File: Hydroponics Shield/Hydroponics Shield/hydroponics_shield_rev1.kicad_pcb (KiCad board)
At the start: 2 copper layers, 125 x 64.5 mm, 50 parts, among them CON1 BARREL_JACK, J1 282836-6, J2 282836-6, P1 CONN_01X02, P2 CONN_01X03, P3 CONN_01X04, P4 CONN_01X02, P5 CONN_01X02, P9 0731000105, Q1 2N7000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

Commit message: desktop night changes
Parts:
- moved C2 133.6 mm to (137.7, 82.5), turned to 270 degrees
- moved R17 132.9 mm to (134.4, 95.0)
- moved R18 129.8 mm to (144.5, 91.7), turned to 180 degrees
- moved C1 125.0 mm to (147.6, 92.7)
- moved U1 118.8 mm to (142.7, 88.9), turned to 90 degrees
- moved R13 108.2 mm to (134.4, 78.5)
- moved REF1 107.1 mm to (147.3, 98.3), turned to 0 degrees
- moved R12 98.3 mm to (144.5, 75.2), turned to 180 degrees
- moved R10 35.0 mm to (100.8, 115.1), turned to 0 degrees
- moved Q6 25.4 mm to (66.5, 97.5), turned to 180 degrees
- moved D3 25.2 mm to (31.0, 93.5), turned to 0 degrees
- moved Q5 24.2 mm to (81.8, 97.5), turned to 180 degrees
- moved Q8 23.6 mm to (36.1, 97.5), turned to 180 degrees
- moved Q7 23.0 mm to (51.3, 97.5), turned to 180 degrees
- moved R6 22.3 mm to (106.2, 88.6), turned to 90 degrees
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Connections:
- net Net-(P9-Pad2) renamed Vguard
- Q4 pad 1: Net-(PCB1-Pad3) -> Net-(PCB1-Pad2)
- R10 pad 2: Net-(PCB1-Pad2) -> Net-(PCB1-Pad3)
- R7 pad 1: Net-(PCB1-Pad3) -> Net-(PCB1-Pad2)
- R9 pad 1: Net-(PCB1-Pad2) -> Net-(PCB1-Pad3)
- SHIELD1 pad 10: DOSING_PUMP_2 -> DOSING_PUMP_1
- SHIELD1 pad 11: DOSING_PUMP_1 -> LED_STRIP_OUT
- SHIELD1 pad 6: LED_STRIP_OUT -> MAIN_PUMP
- SHIELD1 pad 9: MAIN_PUMP -> DOSING_PUMP_2
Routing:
- net MAIN_PUMP: track 0.00 -> 79.0 mm
- net DOSING_PUMP_2: track 0.00 -> 65.2 mm
- net BLE_DATA_TRANSMIT: track 0.00 -> 62.6 mm
- net Vguard: track 0.00 -> 61.3 mm
- net BLE_DATA_RECEIVE: track 0.00 -> 59.2 mm, vias 0 -> 1
- net DOSING_PUMP_1: track 0.00 -> 48.8 mm
- net LED_B: track 0.00 -> 30.5 mm, vias 0 -> 1
- net LED_STRIP_OUT: track 0.00 -> 29.7 mm
- net +5V: track 0.00 -> 25.3 mm
- net LED_R: track 0.00 -> 25.2 mm
- net LED_G: track 0.00 -> 20.2 mm, vias 0 -> 1
- net Net-(C1-Pad1): track 0.00 -> 17.9 mm
- net Net-(Q1-Pad3): track 0.00 -> 15.4 mm
- net PH_VOUT: track 0.00 -> 13.4 mm
- net Net-(Q2-Pad3): track 0.00 -> 10.8 mm
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- added copper zone on B.Cu, net GND
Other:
- board size 125 x 64.5 mm -> 125 x 62.2 mm

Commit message: workday additions
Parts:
- CON1: value BARREL_JACK -> PJ-202A
- P1, P4, P5: value CONN_01X02 -> 22-05-3021
- P2: value CONN_01X03 -> 0022053031
- P3: value CONN_01X04 -> 0022053041
- moved P5 53.2 mm to (148.3, 102.4), turned to 0 degrees
- moved J2 4.17 mm to (67.3, 64.3)
- moved J1 3.84 mm to (99.0, 64.3)
- moved CON1 3.49 mm to (36.3, 62.9)
- moved P9 3.05 mm to (149.1, 64.0)
- moved P4 2.34 mm to (108.2, 68.6)
- moved P2 2.34 mm to (122.4, 68.6)
- moved P3 2.30 mm to (132.3, 68.6)
- moved P1 2.29 mm to (115.3, 68.6)
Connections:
- J1 pad 1: GND -> +12V
- J1 pad 2: GND -> +12V
- J1 pad 3: GND -> +12V
- SHIELD1 pad AD0: PH_VOUT -> TEMP_SENSE_IN
- SHIELD1 pad AD1: PH_VREF -> PH_VOUT
- SHIELD1 pad AD2: TEMP_SENSE_IN -> Vguard
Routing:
- net +12V: track 0.00 -> 205.4 mm
- net +5V: track 25.3 -> 167.3 mm, vias 0 -> 3
- net AUX_BTTN1_IN: track 4.87 -> 105.2 mm, vias 0 -> 3
- net TEMP_SENSE_IN: track 0.00 -> 86.4 mm, vias 0 -> 4
- net PH_VOUT: track 13.4 -> 81.5 mm, vias 0 -> 1
- net Vguard: track 61.3 -> 120.3 mm, vias 0 -> 1
- net +3V3: track 0.00 -> 54.5 mm, vias 0 -> 2
- net Net-(J1-Pad4): track 0.00 -> 45.3 mm
- net Net-(C5-Pad2): track 0.00 -> 42.1 mm
- net Net-(C3-Pad2): track 0.90 -> 41.3 mm
- net Net-(C4-Pad2): track 0.00 -> 39.9 mm
- net Net-(PCB1-Pad2): track 5.75 -> 41.4 mm, vias 0 -> 2
- net GND: track 0.00 -> 24.7 mm, vias 0 -> 1
- net Net-(P3-Pad1): track 5.03 -> 21.2 mm, vias 1 -> 0
- net Net-(P3-Pad2): track 3.47 -> 19.7 mm
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- added copper zone on F.Cu, net GND
- added copper zone on B.Cu, net Vguard
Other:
- board size 125 x 62.2 mm -> 125 x 65.5 mm
- board text added: "+"
- board text added: "+12V IN"
- board text added: "-"
- board text added: "- OUT +"
- board text added: "AUX BTTN"
- board text added: "B G R A"
- board text added: "BTTN"
- board text added: "DOSING PUMP 1"
- board text added: "DOSING PUMP 2"
- board text added: "FLOAT SWITCH"
- board text added: "GROW LIGHTS"
- board text added: "HC05 Bluetooth Module"
- board text added: "HYDROPONICS SHIELD V0.1"
- board text added: "MAIN PUMP"
- board text added: "PH PROBE"
- board text added: "RGB LED"
- board text added: "TEMP SENSE"

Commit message: changes made extra pump wifi
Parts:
- added C6: 5ZLH100MEFC6.3X11, Capacitors_ThroughHole:C_Radial_D6.3_L11.2_P2.5, F.Cu at (65.0, 87.9)
- added D4: 1N4148, Diodes_ThroughHole:Diode_DO-35_SOD27_Horizontal_RM10, F.Cu at (61.0, 93.5)
- added Q9: PSMN022-30PL,127, TO_SOT_Packages_THT:TO-220_Neutral123_Horizontal_LargePads, F.Cu at (66.5, 97.5)
- added R22: 10.0k, Resistors_ThroughHole:Resistor_Horizontal_RM10mm, F.Cu at (102.9, 88.6)
- PCB1: value HC05_BLUETOOTH -> ESP8266; footprint USER_MODULES:HC05_BLUETOOTH_SMD -> USER_MODULES:ESP8266
- moved R16 19.8 mm to (83.1, 88.6)
- moved R9 17.0 mm to (126.2, 119.4)
- moved R7 16.2 mm to (126.2, 112.8)
- moved PCB1 15.9 mm to (131.8, 117.1), turned to 0 degrees
- moved R10 15.3 mm to (116.1, 116.1)
- moved C4 15.2 mm to (35.1, 87.9)
- moved C5 15.2 mm to (19.3, 87.9)
- moved D1 15.2 mm to (46.2, 93.5)
- moved D3 15.2 mm to (15.7, 93.5)
- moved Q6 15.2 mm to (51.3, 97.5)
- moved Q7 15.2 mm to (36.1, 97.5)
- moved D2 15.2 mm to (31.0, 93.5)
- moved Q8 15.2 mm to (20.8, 97.5)
- moved C3 15.2 mm to (50.3, 87.9)
- moved Q4 13.7 mm to (118.6, 105.7)
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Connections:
- net BLE_DATA_RECEIVE renamed WIFI_DATA_RECEIVE
- net BLE_DATA_TRANSMIT renamed WIFI_DATA_TRANSMIT
- J1 pad 3: +12V -> Net-(J1-Pad3)
- J1 pad 4: Net-(J1-Pad4) -> Net-(J1-Pad3)
- J1 pad 5: Net-(J1-Pad4) -> Net-(C6-Pad2)
- J1 pad 6: Net-(J1-Pad4) -> +12V
- PCB1 pad 1: Net-(PCB1-Pad1) -> GND
- PCB1 pad 4: GND -> +3V3
- PCB1 pad 5: +5V -> Net-(PCB1-Pad5)
- Q5 pad 2: Net-(J1-Pad4) -> Net-(J1-Pad3)
- R10 pad 2: Net-(PCB1-Pad3) -> Net-(PCB1-Pad7)
- R9 pad 1: Net-(PCB1-Pad3) -> Net-(PCB1-Pad7)
- SHIELD1 pad 12: Net-(SHIELD1-Pad12) -> MAIN_PUMP
- SHIELD1 pad 6: MAIN_PUMP -> TOPUP_PUMP
- SHIELD1 pad GND3: Net-(SHIELD1-PadGND3) -> GND
- SHIELD1 pad V_IN: Net-(SHIELD1-PadV_IN) -> +12V
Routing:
- net AUX_BTTN1_IN: track 105.2 -> 4.87 mm, vias 3 -> 0
- net +12V: track 205.4 -> 132.0 mm
- net TOPUP_PUMP: track 0.00 -> 48.4 mm
- net Net-(J1-Pad3): track 0.00 -> 47.8 mm
- net Net-(J1-Pad4): track 45.3 -> 0.00 mm
- net Net-(C6-Pad2): track 0.00 -> 44.2 mm
- net WIFI_DATA_RECEIVE: track 59.7 -> 34.1 mm, vias 1 -> 0
- net Net-(PCB1-Pad2): track 41.4 -> 19.1 mm, vias 2 -> 0
- net +5V: track 167.3 -> 149.2 mm, vias 3 -> 0
- net +3V3: track 54.5 -> 71.0 mm, vias 2 -> 0
- net DOSING_PUMP_1: track 48.8 -> 62.8 mm
- net DOSING_PUMP_2: track 65.2 -> 77.1 mm
- net WIFI_DATA_TRANSMIT: track 63.7 -> 52.6 mm
- net Net-(PCB1-Pad7): track 0.00 -> 10.8 mm
- net Net-(C5-Pad2): track 42.1 -> 52.6 mm
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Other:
- board size 125 x 65.5 mm -> 140.5 x 67.1 mm
- board text added: "TOP-UP PUMP"
- board text removed: "HC05 Bluetooth Module"

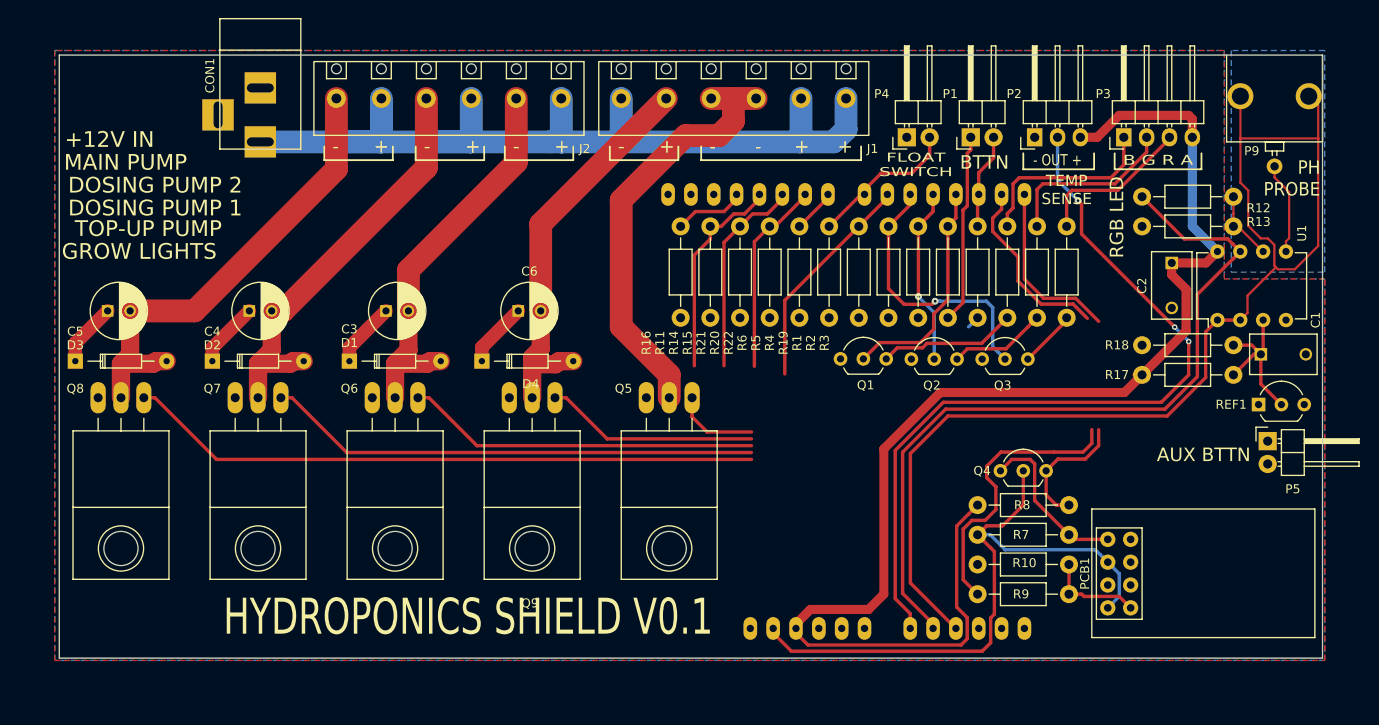
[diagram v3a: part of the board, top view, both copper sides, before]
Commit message: finished board change from bt to wifi
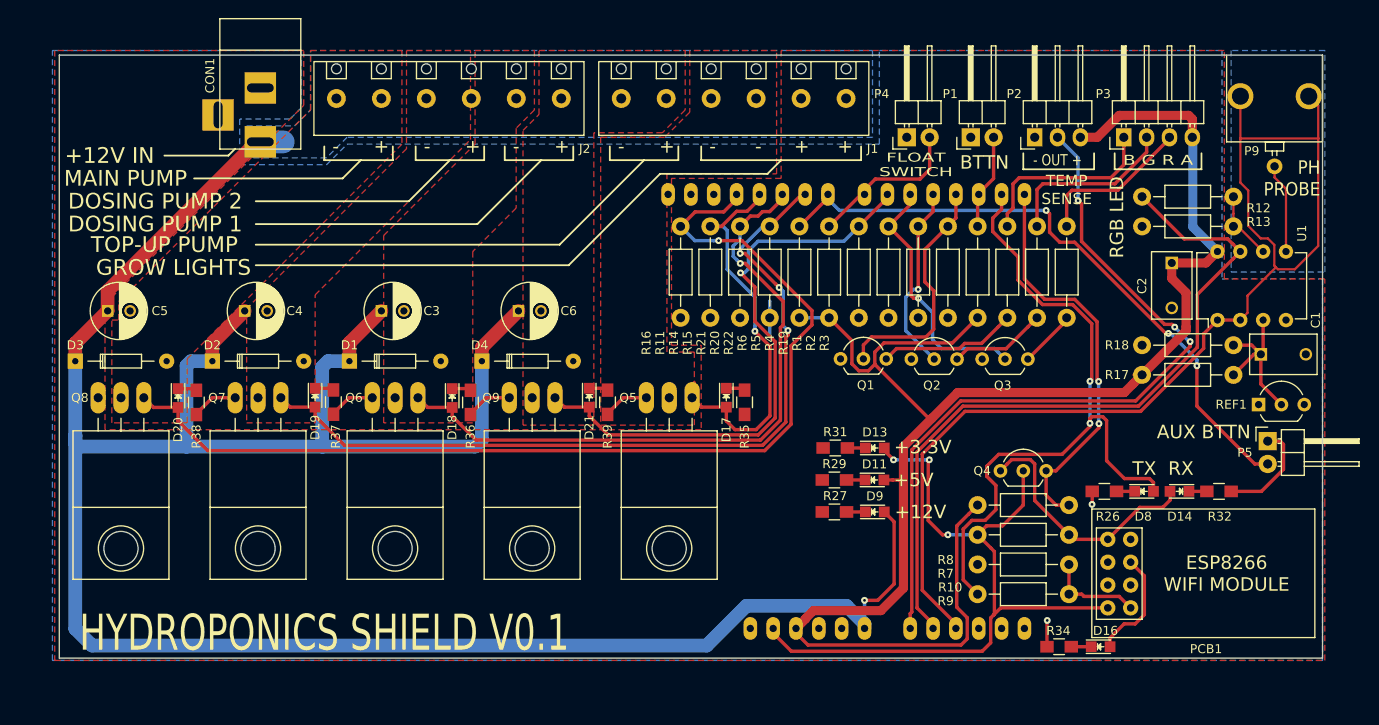
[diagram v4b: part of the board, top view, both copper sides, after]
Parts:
- added D11: GN, LEDs:LED_0805, F.Cu at (104.6, 106.7)
- added D13: GN, LEDs:LED_0805, F.Cu at (104.6, 103.1)
- added D14: GN, LEDs:LED_0805, F.Cu at (138.5, 108.0)
- added D16: GN, LEDs:LED_0805, F.Cu at (129.8, 125.2)
- added D17: GN, LEDs:LED_0805, F.Cu at (88.1, 97.5)
- added D18: GN, LEDs:LED_0805, F.Cu at (57.7, 97.6)
- added D19: GN, LEDs:LED_0805, F.Cu at (42.4, 97.5)
- added D20: GN, LEDs:LED_0805, F.Cu at (27.2, 97.6)
- added D21: GN, LEDs:LED_0805, F.Cu at (72.9, 97.5)
- added D8: GN, LEDs:LED_0805, F.Cu at (134.6, 108.0)
- added D9: GN, LEDs:LED_0805, F.Cu at (104.6, 110.2)
- added R26: 500, Resistors_SMD:R_0805_HandSoldering, F.Cu at (130.2, 108.0)
- added R27: 1.0k, Resistors_SMD:R_0805_HandSoldering, F.Cu at (100.2, 110.2)
- added R29: 500, Resistors_SMD:R_0805_HandSoldering, F.Cu at (100.2, 106.7)
- added R31: 200, Resistors_SMD:R_0805_HandSoldering, F.Cu at (100.2, 103.1)
- added R32: 200, Resistors_SMD:R_0805_HandSoldering, F.Cu at (142.9, 108.0)
- added R34: 200, Resistors_SMD:R_0805_HandSoldering, F.Cu at (125.1, 125.2)
- added R35: 500, Resistors_SMD:R_0805_HandSoldering, F.Cu at (90.2, 98.0)
- added R36: 500, Resistors_SMD:R_0805_HandSoldering, F.Cu at (59.7, 98.1)
- added R37: 500, Resistors_SMD:R_0805_HandSoldering, F.Cu at (44.5, 98.0)
- added R38: 500, Resistors_SMD:R_0805_HandSoldering, F.Cu at (29.2, 98.1)
- added R39: 500, Resistors_SMD:R_0805_HandSoldering, F.Cu at (74.9, 98.0)
- moved C3 0.51 mm to (49.8, 87.9)
- moved C4 0.51 mm to (34.6, 87.9)
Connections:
- PCB1 pad 4: +3V3 -> Net-(PCB1-Pad4)
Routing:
- net +12V: track 132.0 -> 273.8 mm, vias 0 -> 1
- net AUX_BTTN1_IN: track 4.87 -> 70.7 mm, vias 0 -> 3
- net Net-(C5-Pad2): track 52.6 -> 0.00 mm
- net Net-(J1-Pad3): track 47.8 -> 0.00 mm
- net Net-(C4-Pad2): track 47.0 -> 0.00 mm
- net Net-(C6-Pad2): track 44.2 -> 0.00 mm
- net Net-(C3-Pad2): track 45.0 -> 0.90 mm
- net MAIN_PUMP: track 78.4 -> 116.6 mm, vias 0 -> 1
- net +5V: track 149.2 -> 185.2 mm
- net WIFI_DATA_TRANSMIT: track 52.6 -> 78.1 mm, vias 0 -> 2
- net GND: track 21.1 -> 40.4 mm, vias 0 -> 2
- net TOPUP_PUMP: track 48.4 -> 66.6 mm, vias 0 -> 1
- net DOSING_PUMP_2: track 77.1 -> 92.9 mm, vias 0 -> 3
- net DOSING_PUMP_1: track 62.8 -> 75.6 mm, vias 0 -> 1
- net LED_STRIP_OUT: track 32.9 -> 45.3 mm, vias 0 -> 1
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- added copper zone on B.Cu, net +12V
- added copper zone on F.Cu, net Net-(C3-Pad2)
- added copper zone on F.Cu, net Net-(C4-Pad2)
- added copper zone on F.Cu, net Net-(C5-Pad2)
- added copper zone on F.Cu, net Net-(C6-Pad2)
- added copper zone on F.Cu, net Net-(J1-Pad3)
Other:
- board text added: "+12V"
- board text added: "+3.3V"
- board text added: "+5V"
- board text added: "ESP8266 WIFI MODULE"
- board text added: "RX"
- board text added: "TX"
